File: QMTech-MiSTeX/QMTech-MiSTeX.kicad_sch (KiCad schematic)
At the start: 47 parts, among them J1 RPi_GPIO, J11 Conn_02x06_Top_Bottom, J12 Conn_01x03_Pin, J13 USB_C_Receptacle_USB2.0, J2 MiSTer SDRAM Module, J3 USB_C_Receptacle_USB2.0, J4 Conn_02x32_Odd_Even, J5 Conn_02x32_Odd_Even, J6 Conn_01x06_Pin, J7 Conn_01x03_Pin, J8 Conn_01x03_Pin

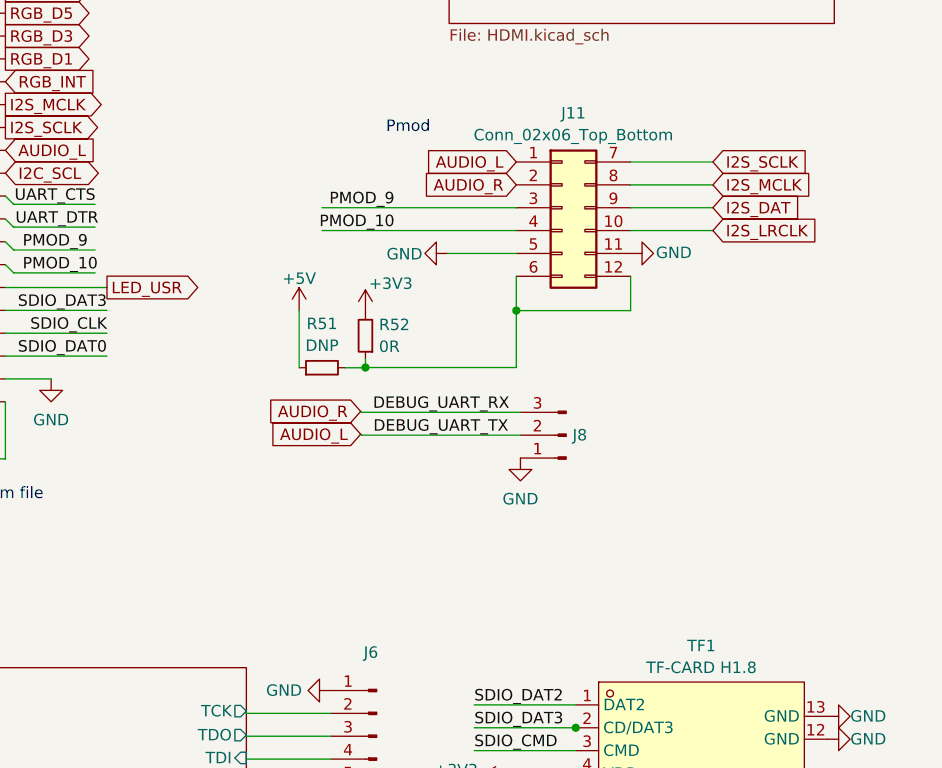
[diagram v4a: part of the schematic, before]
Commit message: Add ESD protection to headphone jack and Pmod
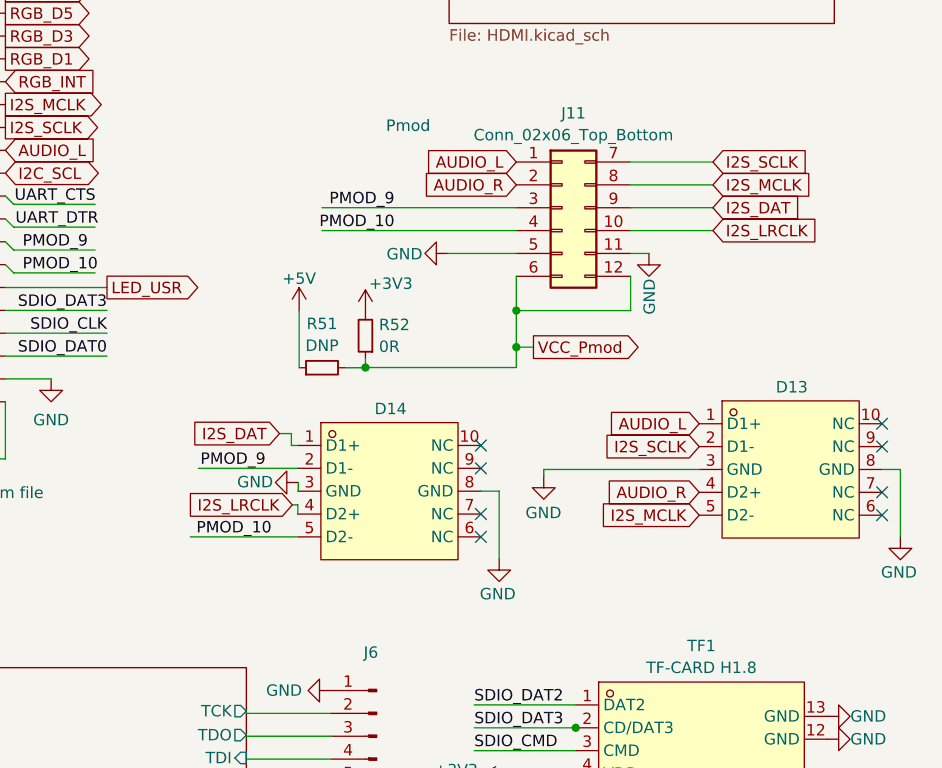
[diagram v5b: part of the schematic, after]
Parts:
- removed J8: Conn_01x03_Pin, Connector_PinHeader_2.54mm:PinHeader_1x03_P2.54mm_Vertical, symbol Connector:Conn_01x03_Pin
- added D13, D14: TPD4E05U06DQAR_C2972498, easyeda2kicad:DFN2510-10_L2.5-W1.0-P0.50-BL, symbol easyeda2kicad:TPD4E05U06DQAR_C2972498
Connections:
- net AUDIO_L: now also D13.1 (D1+)
- net AUDIO_R: now also D13.4 (D2+)
- net GND: now also D13.3 (GND), D13.8 (GND), D14.3 (GND), D14.8 (GND)
- net I2S_DAT: now also D14.1 (D1+)
- net I2S_LRCLK: now also D14.4 (D2+)
- net I2S_MCLK: now also D13.5 (D2-)
- net I2S_SCLK: now also D13.2 (D1-)
- net PMOD_10: now also D14.5 (D2-)
- net PMOD_9: now also D14.2 (D1-)
- net VCC_Pmod: now reaches J11.12 (Pin_12), J11.6 (Pin_6), R51.2, R52.1
- no-connect marks 15 -> 23

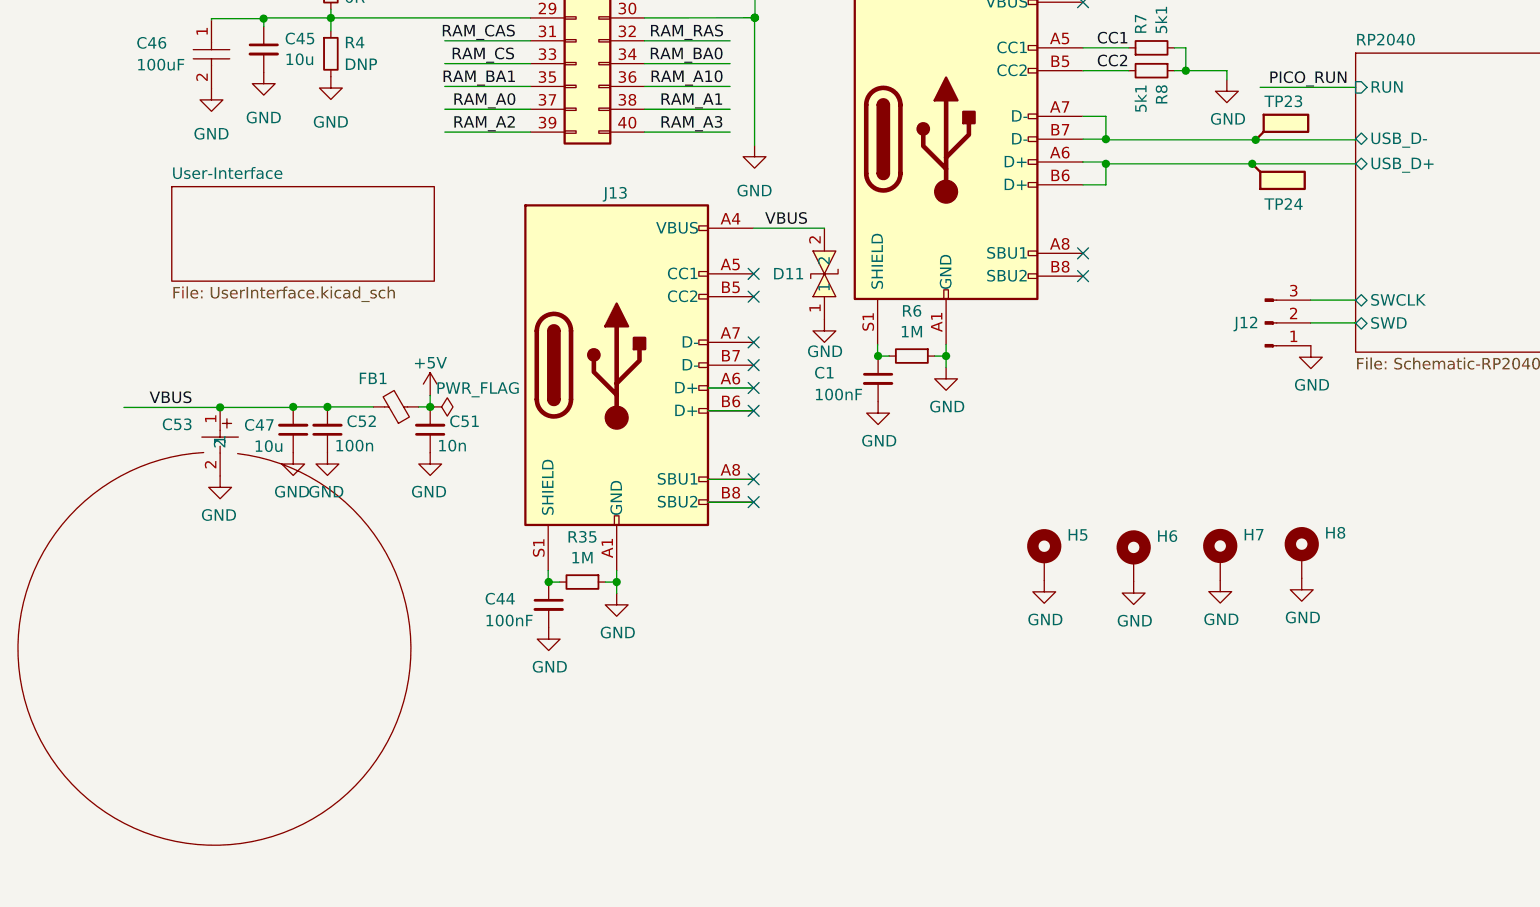
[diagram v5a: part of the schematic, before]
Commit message: add CC1 and CC2 resistors to power connector
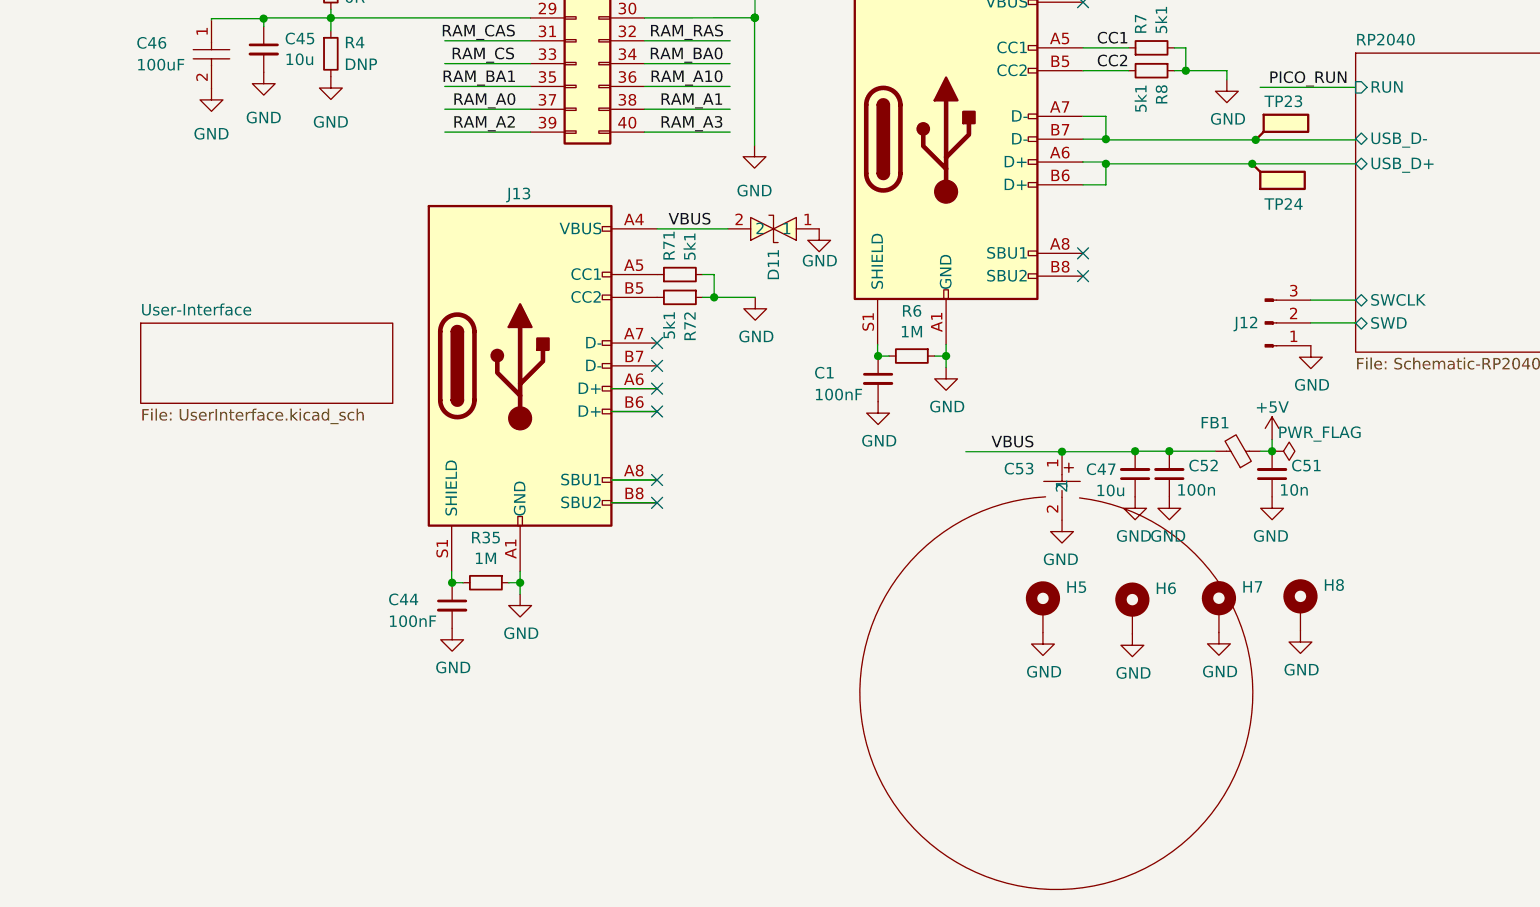
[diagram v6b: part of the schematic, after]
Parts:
- added R71, R72: 5k1, Resistor_SMD:R_0603_1608Metric, symbol Device:R_Small
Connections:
- net GND: now also R71.2, R72.1
- net at J13.A5 (CC1): now also R71.1
- net at J13.B5 (CC2): now also R72.2
- no-connect marks 23 -> 21
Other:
- moved on the sheet: C44, C47, C51, C52, C53, D11, FB1, H5, H6, H7, H8, J13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

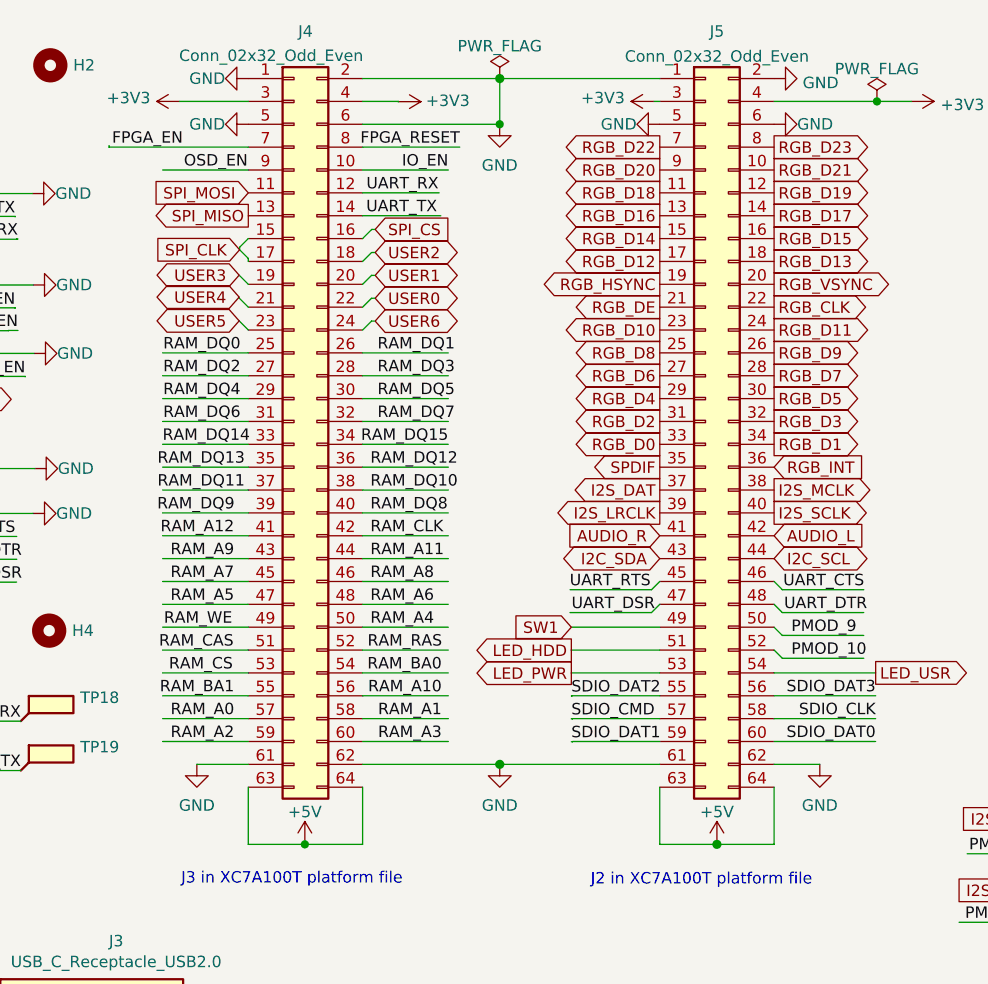
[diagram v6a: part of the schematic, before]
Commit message: Redesign FPGA core board headers to be assembled at the fab
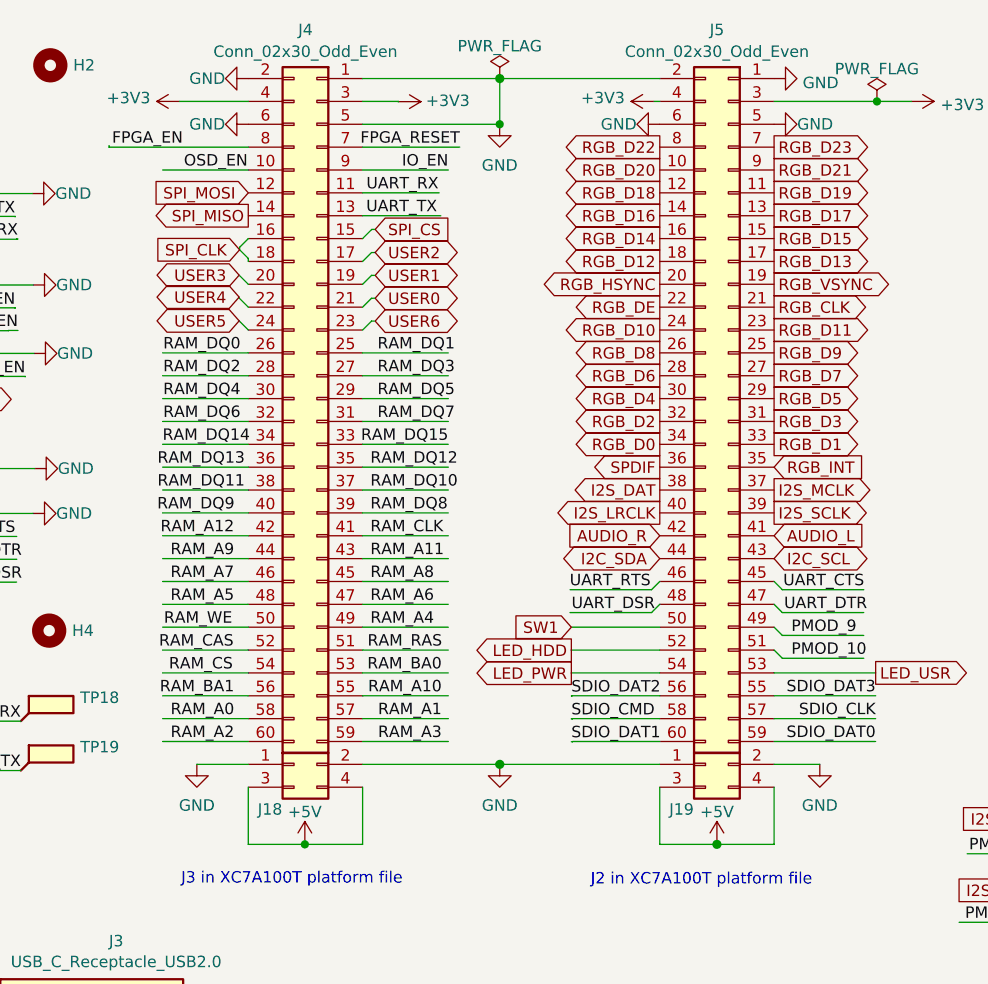
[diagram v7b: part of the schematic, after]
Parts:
- removed J4, J5: Conn_02x32_Odd_Even, Connector_PinHeader_2.54mm:PinHeader_2x32_P2.54mm_Vertical, symbol Connector_Generic:Conn_02x32_Odd_Even
- added J18, J19: Conn_02x02_Odd_Even, Connector_PinSocket_2.54mm:PinSocket_2x02_P2.54mm_Vertical, symbol Connector_Generic:Conn_02x02_Odd_Even
- added J4, J5: Conn_02x30_Odd_Even, Connector_PinSocket_2.54mm:PinSocket_2x30_P2.54mm_Vertical, symbol Connector_Generic:Conn_02x30_Odd_Even
- J2: LCSC (none) -> C429965
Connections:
- net +3V3: now also J4.3 (Pin_3), J4.4 (Pin_4), J5.3 (Pin_3), J5.4 (Pin_4)
- net +5V: now also J18.3 (Pin_3), J18.4 (Pin_4), J19.3 (Pin_3), J19.4 (Pin_4)
- net AUDIO_L: now also J5.41 (Pin_41)
- net AUDIO_R: now also J5.42 (Pin_42)
- net FPGA_EN: now also J4.8 (Pin_8)
- net FPGA_RESET: now also J4.7 (Pin_7)
- net GND: now also J18.1 (Pin_1), J18.2 (Pin_2), J19.1 (Pin_1), J19.2 (Pin_2), J4.1 (Pin_1), J4.2 (Pin_2), J4.5 (Pin_5), J4.6 (Pin_6), J5.1 (Pin_1), J5.2 (Pin_2), J5.5 (Pin_5), J5.6 (Pin_6)
- net I2C_SCL: now also J5.43 (Pin_43)
- net I2C_SDA: now also J5.44 (Pin_44)
- net I2S_DAT: now also J5.38 (Pin_38)
- net I2S_LRCLK: now also J5.40 (Pin_40)
- net I2S_MCLK: now also J5.37 (Pin_37)
- net I2S_SCLK: now also J5.39 (Pin_39)
- net IO_EN: now also J4.9 (Pin_9)
- net LED_HDD: now also J5.52 (Pin_52)
- net LED_PWR: now also J5.54 (Pin_54)
- net LED_USR: now also J5.53 (Pin_53)
- net OSD_EN: now also J4.10 (Pin_10)
- net PMOD_10: now also J5.51 (Pin_51)
- net PMOD_9: now also J5.49 (Pin_49)
- net RAM_A0: now also J4.58 (Pin_58)
- net RAM_A1: now also J4.57 (Pin_57)
- net RAM_A10: now also J4.55 (Pin_55)
- net RAM_A11: now also J4.43 (Pin_43)
- net RAM_A12: now also J4.42 (Pin_42)
- net RAM_A2: now also J4.60 (Pin_60)
- net RAM_A3: now also J4.59 (Pin_59)
- net RAM_A4: now also J4.49 (Pin_49)
- net RAM_A5: now also J4.48 (Pin_48)
- net RAM_A6: now also J4.47 (Pin_47)
- net RAM_A7: now also J4.46 (Pin_46)
- net RAM_A8: now also J4.45 (Pin_45)
- net RAM_A9: now also J4.44 (Pin_44)
- net RAM_BA0: now also J4.53 (Pin_53)
- net RAM_BA1: now also J4.56 (Pin_56)
- net RAM_CAS: now also J4.52 (Pin_52)
- net RAM_CLK: now also J4.41 (Pin_41)
- net RAM_CS: now also J4.54 (Pin_54)
- net RAM_DQ0: now also J4.26 (Pin_26)
- net RAM_DQ1: now also J4.25 (Pin_25)
- net RAM_DQ10: now also J4.37 (Pin_37)
- net RAM_DQ11: now also J4.38 (Pin_38)
- net RAM_DQ12: now also J4.35 (Pin_35)
- net RAM_DQ13: now also J4.36 (Pin_36)
- net RAM_DQ14: now also J4.34 (Pin_34)
- net RAM_DQ15: now also J4.33 (Pin_33)
- net RAM_DQ2: now also J4.28 (Pin_28)
- net RAM_DQ3: now also J4.27 (Pin_27)
- net RAM_DQ4: now also J4.30 (Pin_30)
- net RAM_DQ5: now also J4.29 (Pin_29)
- net RAM_DQ6: now also J4.32 (Pin_32)
- net RAM_DQ7: now also J4.31 (Pin_31)
- net RAM_DQ8: now also J4.39 (Pin_39)
- net RAM_DQ9: now also J4.40 (Pin_40)
- net RAM_RAS: now also J4.51 (Pin_51)
- net RAM_WE: now also J4.50 (Pin_50)
- net RGB_CLK: now also J5.21 (Pin_21)
- net RGB_D0: now also J5.34 (Pin_34)
- net RGB_D1: now also J5.33 (Pin_33)
- net RGB_D10: now also J5.24 (Pin_24)
- net RGB_D11: now also J5.23 (Pin_23)
- net RGB_D12: now also J5.18 (Pin_18)
- net RGB_D13: now also J5.17 (Pin_17)
- net RGB_D14: now also J5.16 (Pin_16)
- net RGB_D15: now also J5.15 (Pin_15)
- net RGB_D16: now also J5.14 (Pin_14)
- net RGB_D17: now also J5.13 (Pin_13)
- net RGB_D18: now also J5.12 (Pin_12)
- net RGB_D19: now also J5.11 (Pin_11)
- net RGB_D2: now also J5.32 (Pin_32)
- net RGB_D20: now also J5.10 (Pin_10)
- net RGB_D21: now also J5.9 (Pin_9)
- net RGB_D22: now also J5.8 (Pin_8)
- net RGB_D23: now also J5.7 (Pin_7)
- net RGB_D3: now also J5.31 (Pin_31)
- net RGB_D4: now also J5.30 (Pin_30)
- net RGB_D5: now also J5.29 (Pin_29)
- net RGB_D6: now also J5.28 (Pin_28)
- net RGB_D7: now also J5.27 (Pin_27)
- net RGB_D8: now also J5.26 (Pin_26)
- net RGB_D9: now also J5.25 (Pin_25)
- net RGB_DE: now also J5.22 (Pin_22)
- net RGB_HSYNC: now also J5.20 (Pin_20)
- net RGB_INT: now also J5.35 (Pin_35)
- net RGB_VSYNC: now also J5.19 (Pin_19)
- net SDIO_CLK: now also J5.57 (Pin_57)
- net SDIO_CMD: now also J5.58 (Pin_58)
- net SDIO_DAT0: now also J5.59 (Pin_59)
- net SDIO_DAT1: now also J5.60 (Pin_60)
- net SDIO_DAT2: now also J5.56 (Pin_56)
- net SDIO_DAT3: now also J5.55 (Pin_55)
- net SPDIF: now also J5.36 (Pin_36)
- net SPI_CLK: now also J4.16 (Pin_16), J4.18 (Pin_18)
- net SPI_CS: now also J4.15 (Pin_15)
- net SPI_MISO: now also J4.14 (Pin_14)
- net SPI_MOSI: now also J4.12 (Pin_12)
- net SW1: now also J5.50 (Pin_50)
- net UART_CTS: now also J5.45 (Pin_45)
- net UART_DSR: now also J5.48 (Pin_48)
- net UART_DTR: now also J5.47 (Pin_47)
- net UART_RTS: now also J5.46 (Pin_46)
- net UART_RX: now also J4.11 (Pin_11)
- net UART_TX: now also J4.13 (Pin_13)
- net USER0: now also J4.21 (Pin_21)
- net USER1: now also J4.19 (Pin_19)
- net USER2: now also J4.17 (Pin_17)
- net USER3: now also J4.20 (Pin_20)
- net USER4: now also J4.22 (Pin_22)
- net USER5: now also J4.24 (Pin_24)
- net USER6: now also J4.23 (Pin_23)
